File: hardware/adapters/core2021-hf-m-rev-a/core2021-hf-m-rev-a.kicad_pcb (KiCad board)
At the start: 2 copper layers, 84 x 80 mm, 28 parts, among them J1 TSW-110-07-G-S, J2 TSW-108-07-G-S, J3 SSQ-108-01-G-S, J4 SSQ-108-01-G-S, U2 AP2112K-3.3TRG1

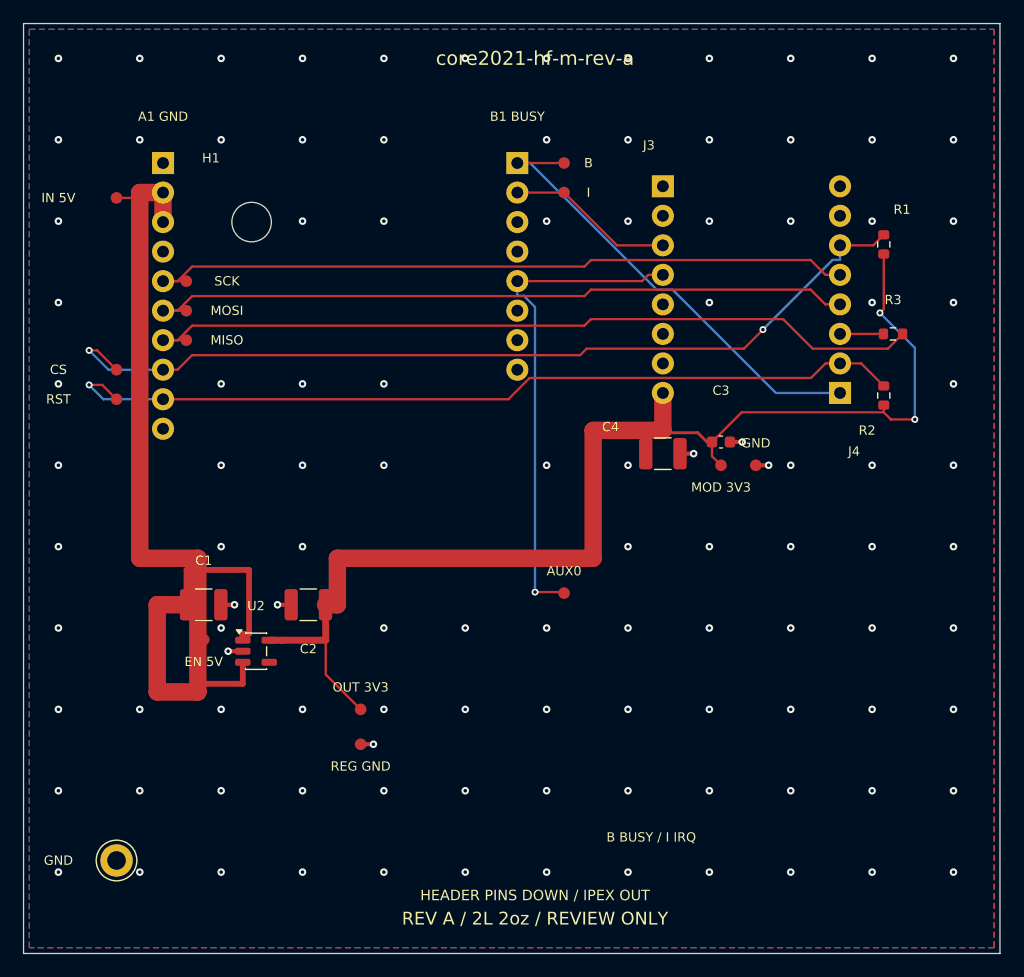
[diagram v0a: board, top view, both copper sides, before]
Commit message: Improve Rev-A ground references and feedback routing
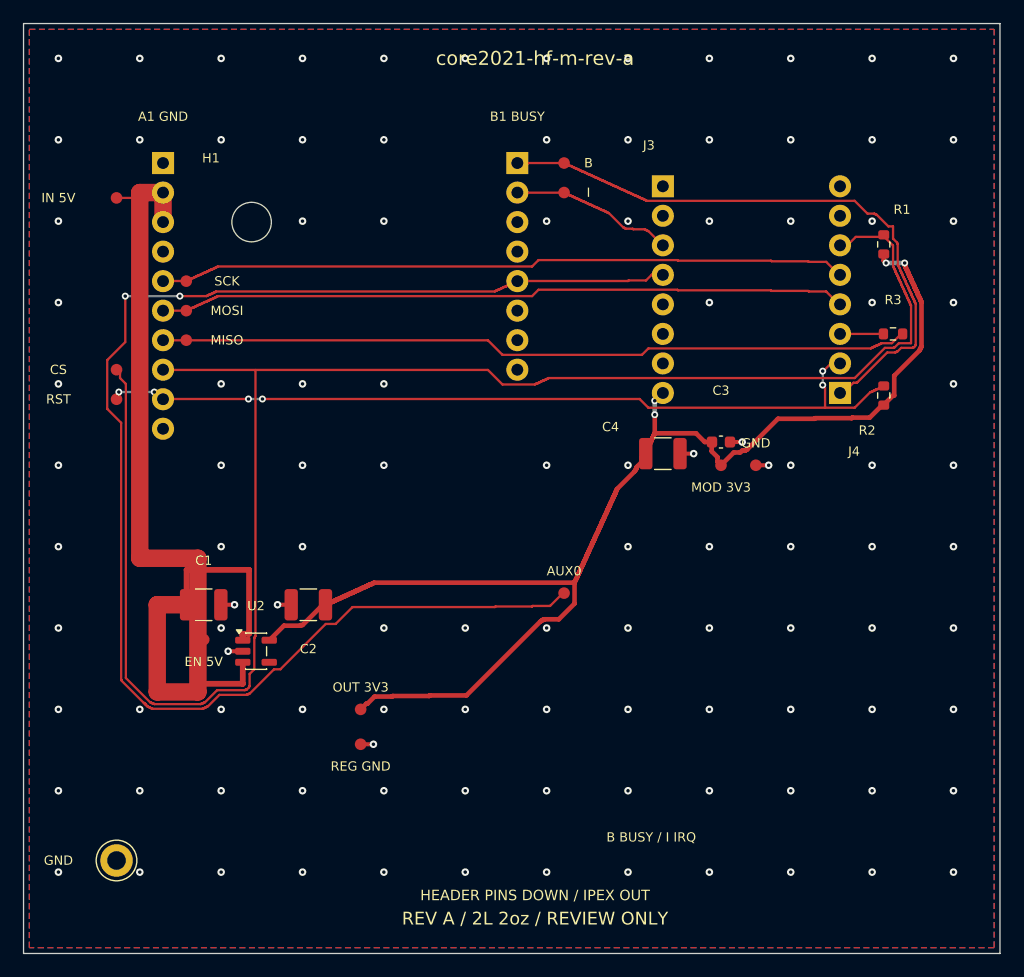
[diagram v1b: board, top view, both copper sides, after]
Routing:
- net /AUX0: track 43.0 -> 124.6 mm, vias 1 -> 2
- net /CS_N: track 77.6 -> 147.2 mm, vias 2 -> 0
- net /BUSY: track 40.1 -> 53.8 mm
- net /RADIO_3V3: track 104.3 -> 112.2 mm, vias 2 -> 4
- net /SPI_MISO: track 68.0 -> 64.9 mm
- net /SPI_MOSI: track 61.5 -> 59.5 mm
- net /SPI_SCK: track 61.5 -> 59.5 mm
- net /RESET_N: track 73.8 -> 72.8 mm, vias 1 -> 6
